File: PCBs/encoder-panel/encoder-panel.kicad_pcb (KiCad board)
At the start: 2 copper layers, 62.2 x 55.9 mm, 42 parts, among them J1 Conn_01x05, U1 EN1AJ-B28

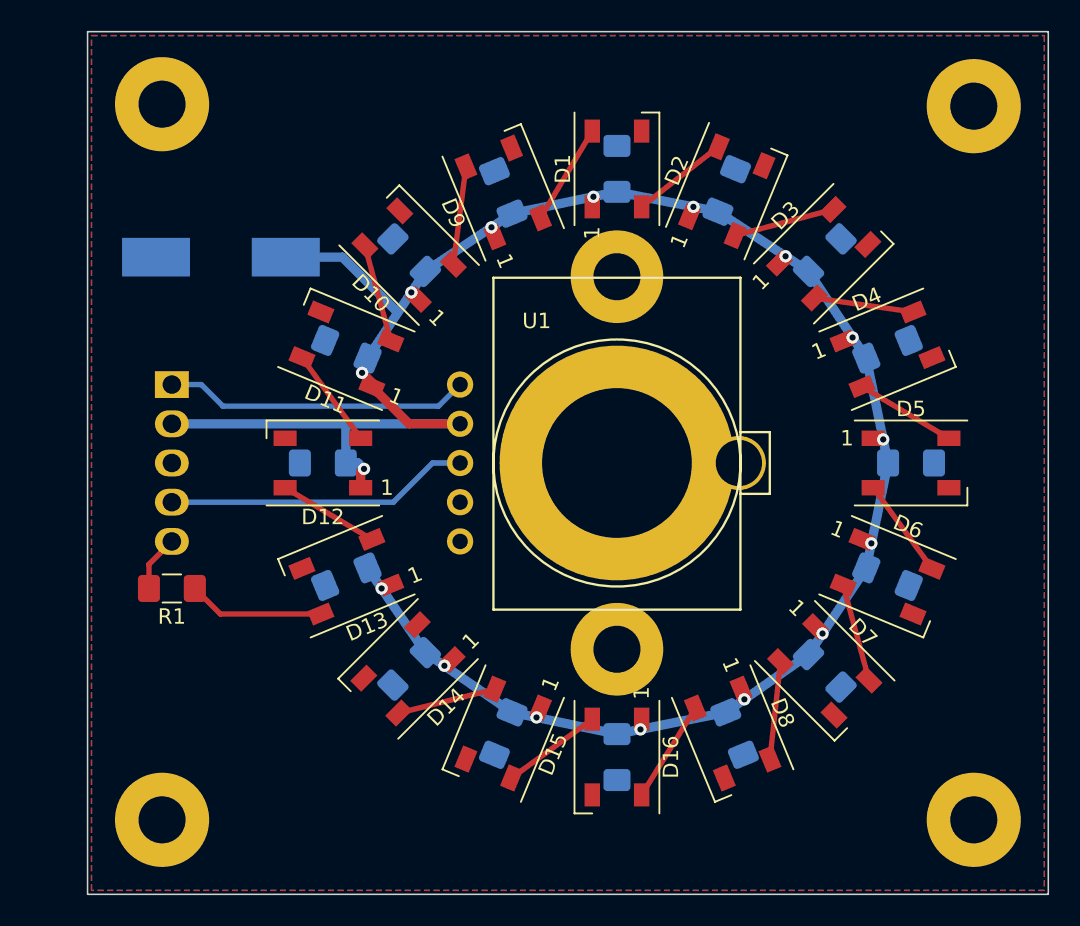
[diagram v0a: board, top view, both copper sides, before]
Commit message: updating encoder panel
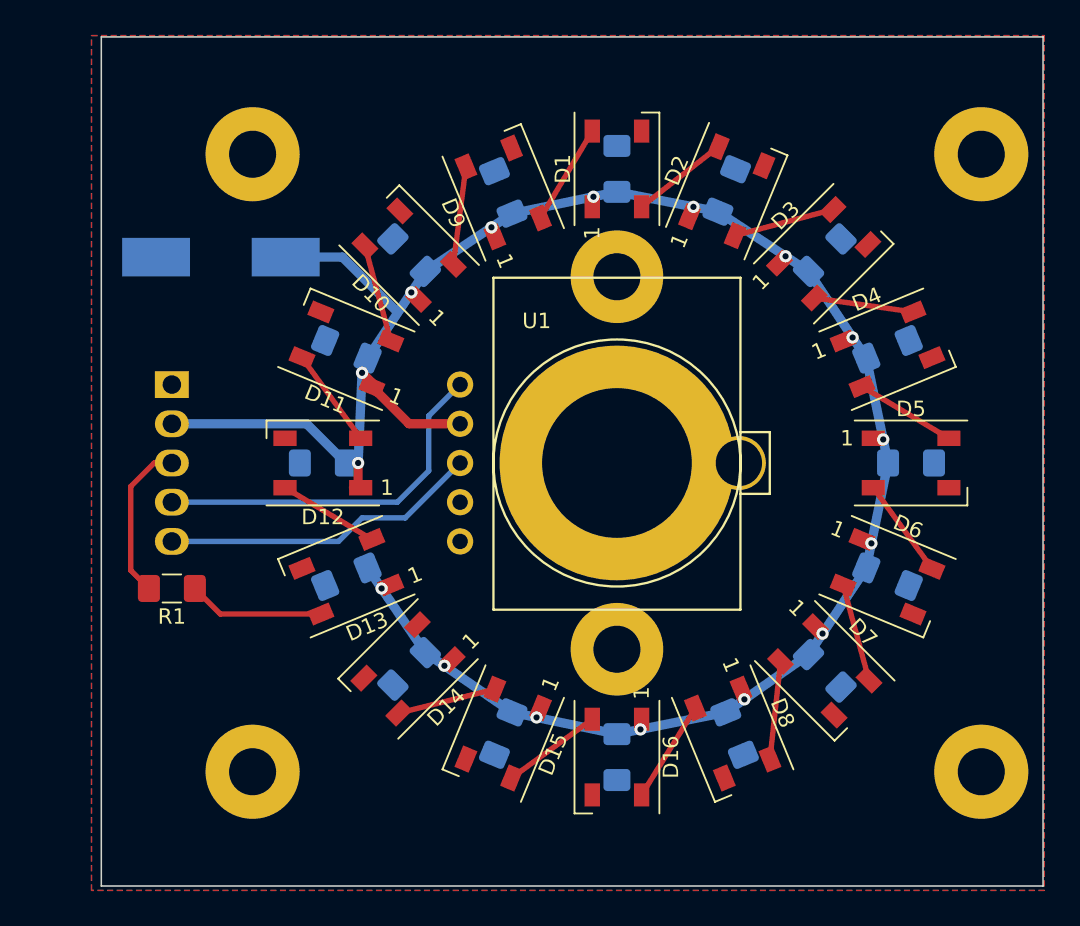
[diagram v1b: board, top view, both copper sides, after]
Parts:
- moved MH3 6.70 mm to (128.8, 81.6)
- moved MH5 6.64 mm to (128.8, 121.6)
- moved MH6 3.15 mm to (176.0, 121.6)
- moved MH4 3.15 mm to (176.0, 81.6)
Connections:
- J1 pad 1: Net-(J1-Pad1) -> GND
- J1 pad 3: GND -> Net-(J1-Pad3)
- R1 pad 2: Net-(J1-Pad5) -> Net-(J1-Pad3)
- U1 pad 1: Net-(J1-Pad1) -> Net-(J1-Pad4)
- U1 pad 3: Net-(J1-Pad4) -> Net-(J1-Pad5)
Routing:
- net Net-(J1-Pad1): track 19.8 -> 0.00 mm
- net Net-(J1-Pad5): track 3.66 -> 20.8 mm
- net Net-(J1-Pad3): track 0.00 -> 10.4 mm
- net Net-(J1-Pad4): track 19.7 -> 23.9 mm
- net +5V: track 137.6 -> 134.4 mm
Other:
- board size 62.2 x 55.9 mm -> 61 x 55 mm
- rule pad_to_mask_clearance: 0.2 -> 0.0508
- board text added: "PXL"
- board text removed: "NeoPxl"

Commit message: tidying up footprints
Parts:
- U1: value EN1AJ-B28 -> ENA1J-B28; footprint Bournes-EN:EN1AJ-B28-L100128L-H -> encoder-panel:ENA1J-B28-L00128L
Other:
- board text added: "version 1.1"
- board text removed: "version 1.0"

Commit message: finishing
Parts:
- added C18: 1000uF, Capacitor_SMD:CP_Elec_8x5.4, B.Cu at (121.9, 114.9)
- added C19: 1000uF, Capacitor_THT:CP_Radial_D8.0mm_P5.00mm, B.Cu at (121.9, 85.7)
- added C20: 1000uF, Capacitor_THT:CP_Radial_D8.0mm_P5.00mm, B.Cu at (121.9, 117.5)
- added LOGO1: Logo_Open_Hardware_Small, Symbol:OSHW-Logo2_9.8x8mm_SilkScreen, B.Cu at (137.2, 124.2)
- added LOGO2: Logo_Open_Hardware_Small, Symbol:OSHW-Logo2_9.8x8mm_SilkScreen, F.Cu at (168.4, 124.5)
- C17: footprint Capacitor_SMD:CP_Elec_10x10.5 -> Capacitor_SMD:CP_Elec_8x5.4
- moved C17 4.83 mm to (121.9, 88.1), turned to 270 degrees
- moved R1 2.30 mm to (121.3, 109.5)
- moved J1 2.29 mm to (121.3, 96.5)
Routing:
- net +5V: track 134.4 -> 162.6 mm
- net Net-(J1-Pad5): track 20.8 -> 23.2 mm
- net Net-(J1-Pad4): track 23.9 -> 26.3 mm
- net Net-(D13-Pad4): track 8.85 -> 11.2 mm
- net Net-(J1-Pad3): track 10.4 -> 9.72 mm
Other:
- board size 61 x 55 mm -> 64 x 55 mm
- board text added: "NPxl"
- board text added: "github.com/FutureSharks/preamp-two"
- board text removed: "PXL"
